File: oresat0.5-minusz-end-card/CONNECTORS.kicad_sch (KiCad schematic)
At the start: 25 parts, among them J2 Harwin M55-7101242R, J3 Harwin M55-7101242R, J4 Harwin M55-7101242R, J5 Harwin M55-7101242R

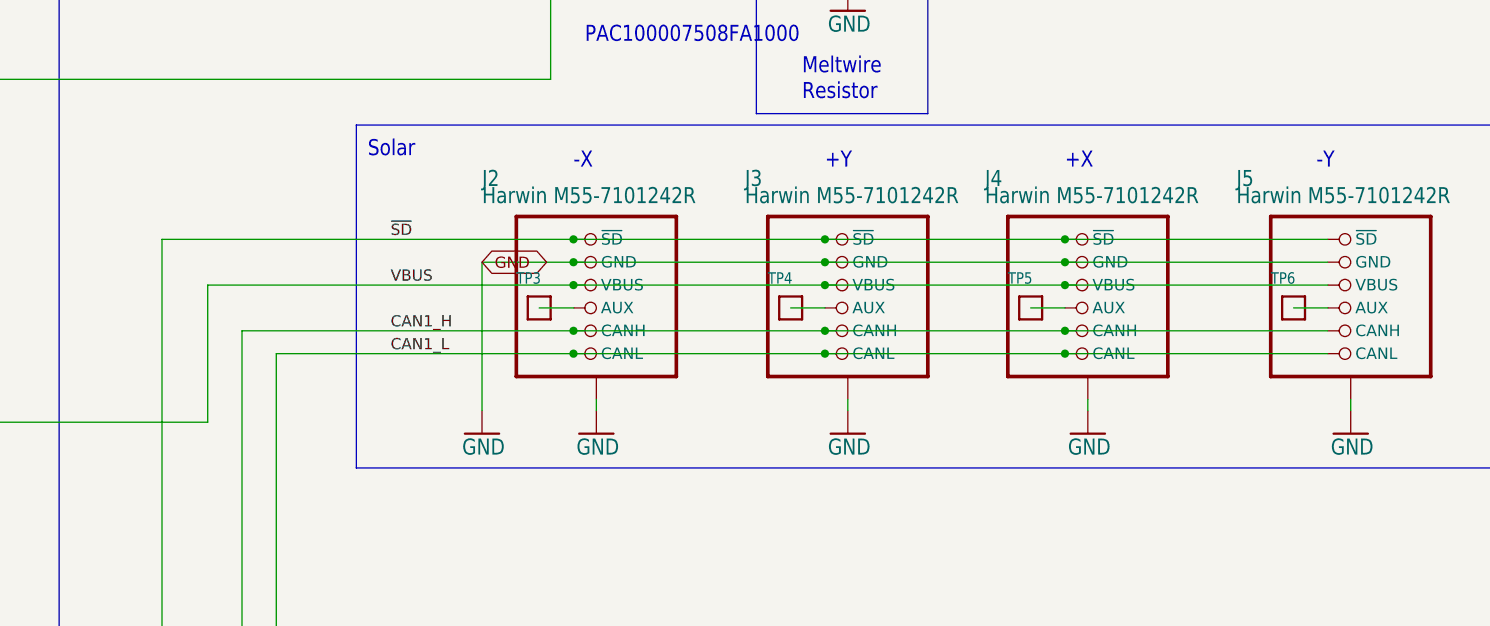
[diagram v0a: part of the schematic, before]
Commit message: Added new outline
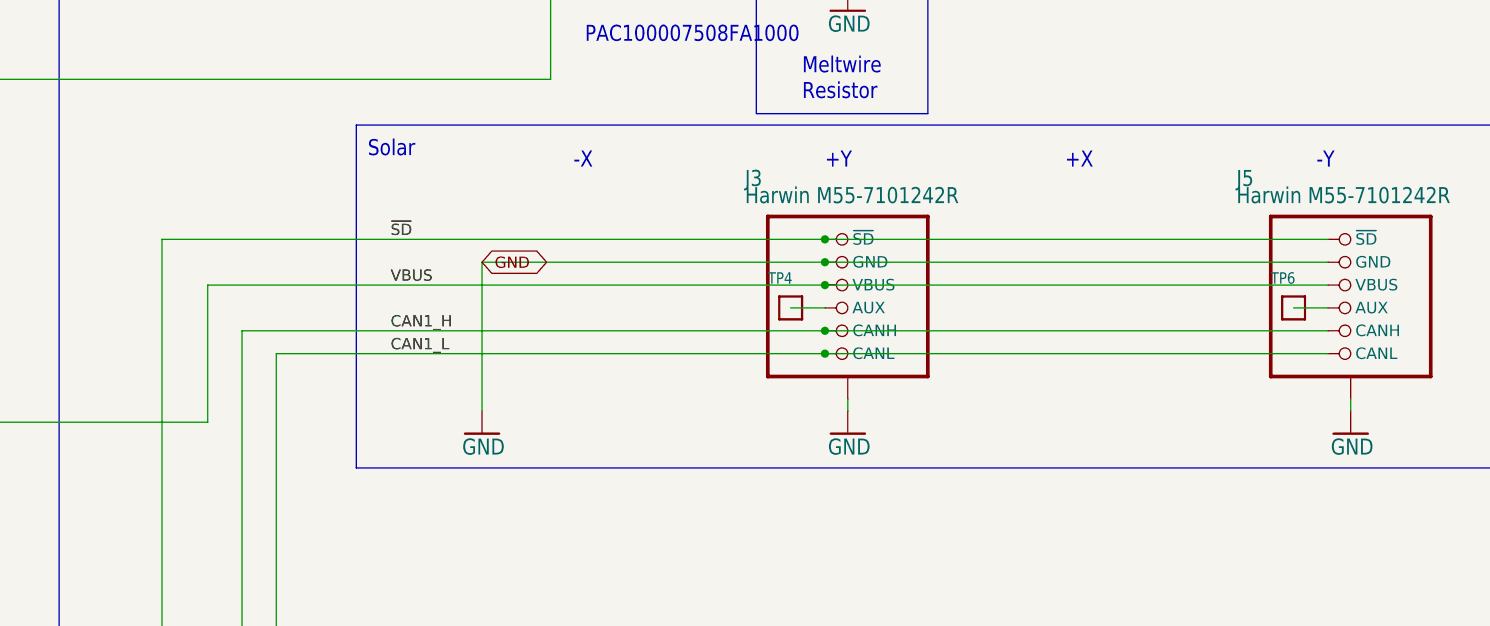
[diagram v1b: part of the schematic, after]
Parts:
- removed J2, J4: Harwin M55-7101242R, oresat-footprints:J-Harwin-M55-7101242R, symbol OreSat-j-solar-card-connector:SOLAR-CARD-CONNECTOR
- removed TP3, TP5: TEST-POINT-LARGE-SQUARE, plusz-end-card-with-turnstile:1X01, symbol plusz-end-card-with-turnstile-eagle-import:TEST-POINT-LARGE-SQUARE

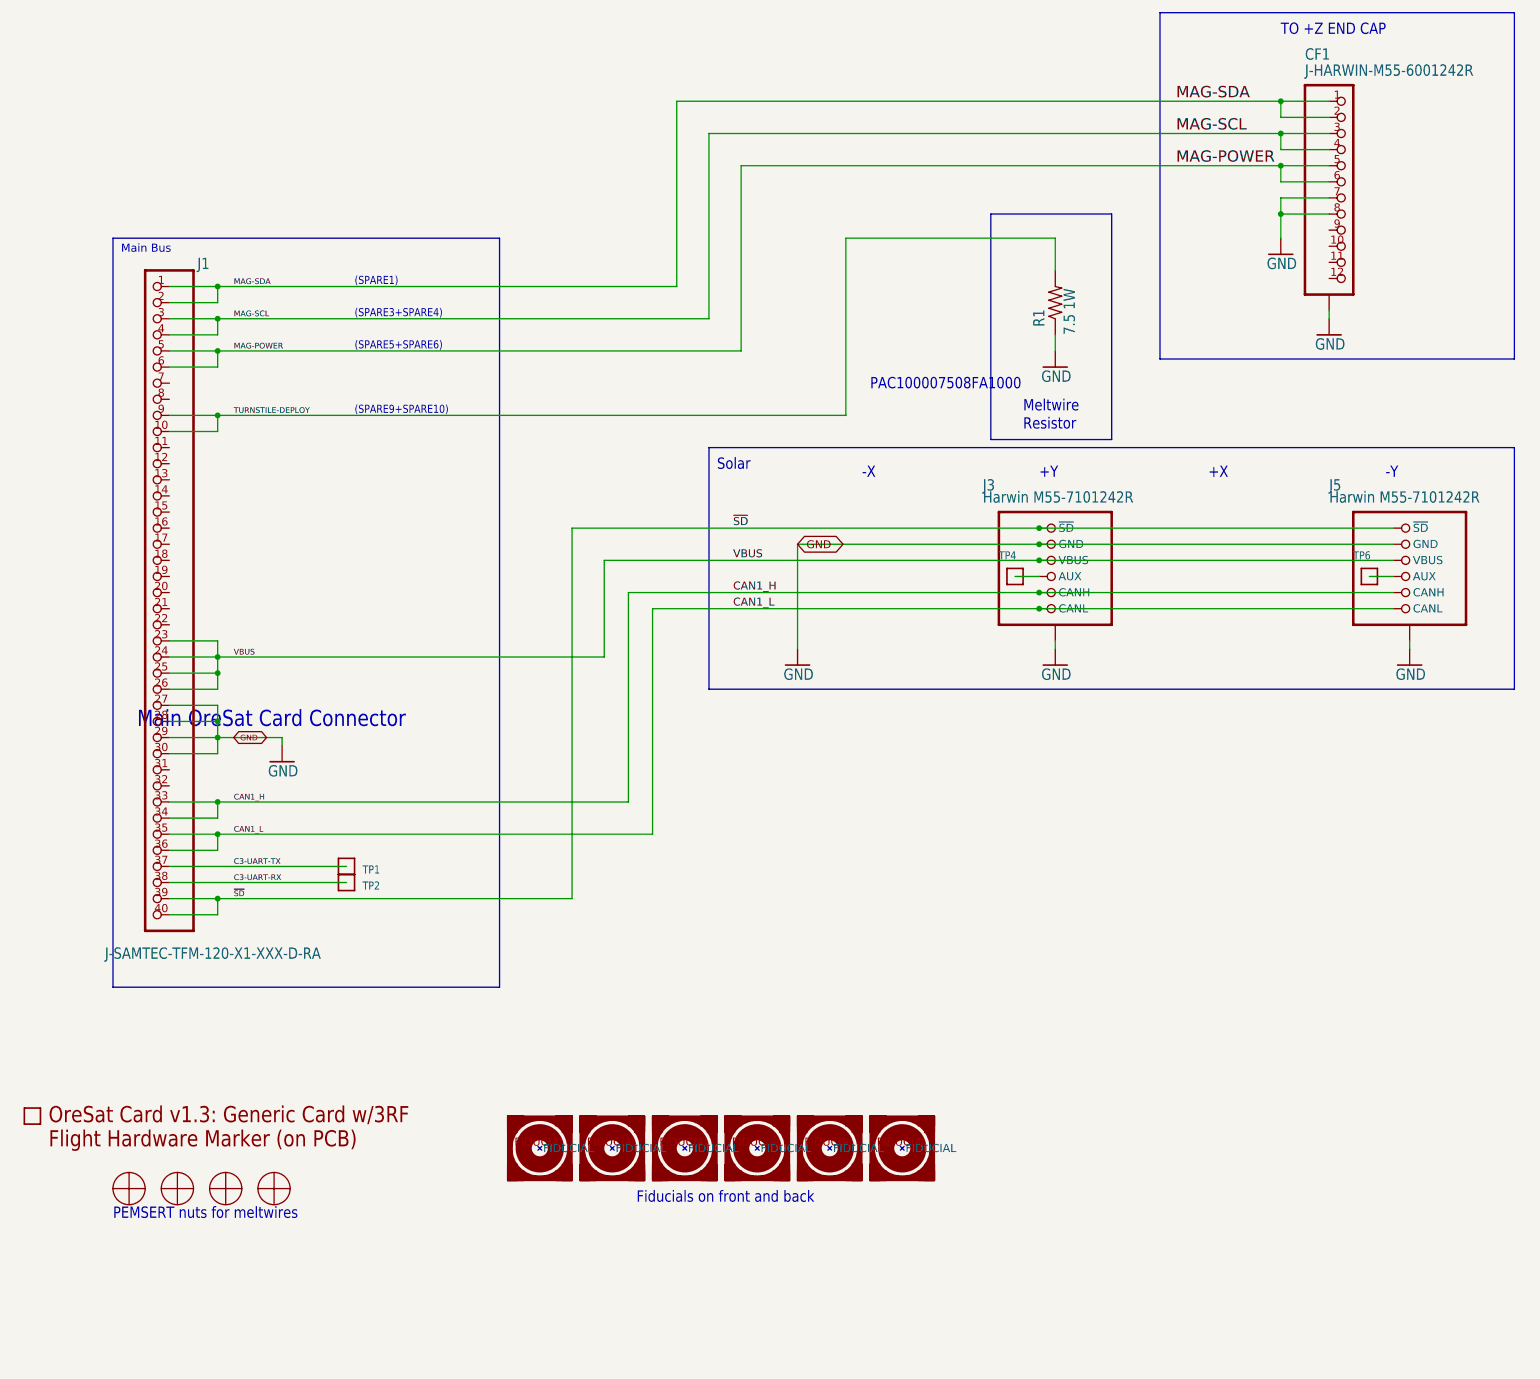
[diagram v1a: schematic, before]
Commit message: Updated -Z end card and replaced eagle imported libraries with kicad libraries
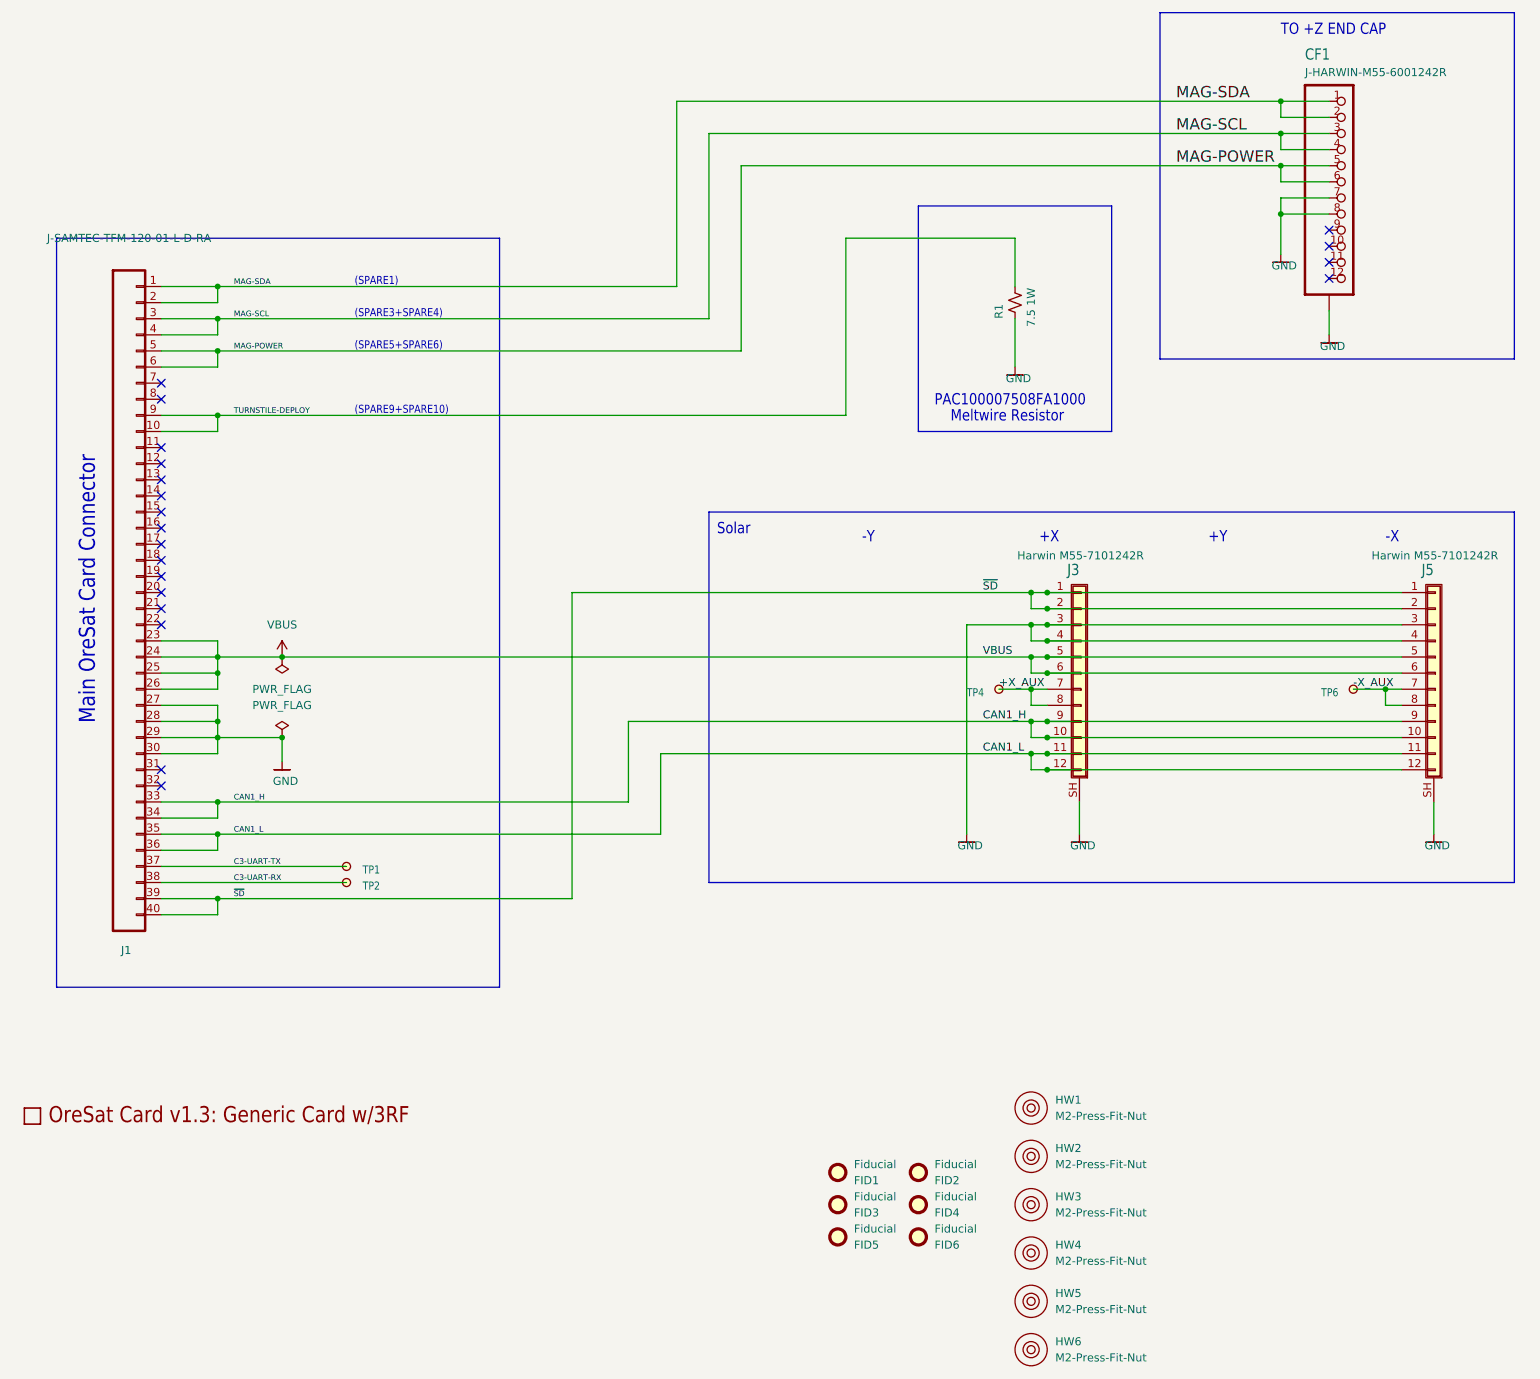
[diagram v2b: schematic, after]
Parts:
- removed HW1, HW2, HW3, HW4: MCMASTER-94100A150, oresat-footprints:H-MCMASTER-94100A150, symbol plusz-end-card-with-turnstile-eagle-import:MCMASTER-94100A150
- removed R1: 7.5 1W, oresat-footprints:R-PAC100-FOR-MELTWIRE, symbol plusz-end-card-with-turnstile-eagle-import:PAC100-FOR-MELTWIRE
- removed U$1: FLIGHMARKERNEW, plusz-end-card-with-turnstile:FLIGHTMARKER_NEW_BOARDS, symbol plusz-end-card-with-turnstile-eagle-import:FLIGHMARKERNEW
- added HW1, HW2, HW3, HW4, HW5, HW6: M2-Press-Fit-Nut, oresat-misc:M2-Press-Fit-Nut, symbol oresat-misc:M2-Press-Fit-Nut
- added R1: 7.5 1W, oresat-passives:R-PAC100-FOR-MELTWIRE, symbol Device:R_Small_US
- CF1: footprint plusz-end-card-with-turnstile:HARWIN-M55-60X1242R -> oresat-connectors:J-Harwin-M55-60X1242R; symbol plusz-end-card-with-turnstile-eagle-import:J-HARWIN-M55-60X1242R -> oresat-connectors:J-HARWIN-M55-6001242R
- FID1: renamed from FIDUCIAL1; value FIDUCIAL-1.0X2.0 -> Fiducial; footprint plusz-end-card-with-turnstile:FIDUCIAL-1.0X2.0 -> Fiducial:Fiducial_1mm_Mask2mm; symbol plusz-end-card-with-turnstile-eagle-import:FIDUCIAL-1.0X2.0 -> Mechanical:Fiducial
- FID2: renamed from FIDUCIAL2; value FIDUCIAL-1.0X2.0 -> Fiducial; footprint plusz-end-card-with-turnstile:FIDUCIAL-1.0X2.0 -> Fiducial:Fiducial_1mm_Mask2mm; symbol plusz-end-card-with-turnstile-eagle-import:FIDUCIAL-1.0X2.0 -> Mechanical:Fiducial
- FID3: renamed from FIDUCIAL3; value FIDUCIAL-1.0X2.0 -> Fiducial; footprint plusz-end-card-with-turnstile:FIDUCIAL-1.0X2.0 -> Fiducial:Fiducial_1mm_Mask2mm; symbol plusz-end-card-with-turnstile-eagle-import:FIDUCIAL-1.0X2.0 -> Mechanical:Fiducial
- FID4: renamed from FIDUCIAL4; value FIDUCIAL-1.0X2.0 -> Fiducial; footprint plusz-end-card-with-turnstile:FIDUCIAL-1.0X2.0 -> Fiducial:Fiducial_1mm_Mask2mm; symbol plusz-end-card-with-turnstile-eagle-import:FIDUCIAL-1.0X2.0 -> Mechanical:Fiducial
- FID5: renamed from FIDUCIAL5; value FIDUCIAL-1.0X2.0 -> Fiducial; footprint plusz-end-card-with-turnstile:FIDUCIAL-1.0X2.0 -> Fiducial:Fiducial_1mm_Mask2mm; symbol plusz-end-card-with-turnstile-eagle-import:FIDUCIAL-1.0X2.0 -> Mechanical:Fiducial
- FID6: renamed from FIDUCIAL6; value FIDUCIAL-1.0X2.0 -> Fiducial; footprint plusz-end-card-with-turnstile:FIDUCIAL-1.0X2.0 -> Fiducial:Fiducial_1mm_Mask2mm; symbol plusz-end-card-with-turnstile-eagle-import:FIDUCIAL-1.0X2.0 -> Mechanical:Fiducial
- J1: value (none) -> J-SAMTEC-TFM-120-01-L-D-RA; symbol plusz-end-card-with-turnstile-eagle-import:J-SAMTEC-TFM-120-X1-XXX-D-RA -> oresat-connectors:J-SAMTEC-TFM-120-01-L-D-RA
- J3, J5: footprint oresat-footprints:J-Harwin-M55-7101242R -> oresat-connectors:J-Harwin-M55-7101242R; symbol OreSat-j-solar-card-connector:SOLAR-CARD-CONNECTOR -> oresat-connectors:Harwin M55-7101242R
- TP1, TP2, TP4, TP6: footprint plusz-end-card-with-turnstile:1X01 -> oresat-misc:TestPoint-MinTH; symbol plusz-end-card-with-turnstile-eagle-import:TEST-POINT-LARGE-SQUARE -> oresat-misc:TestPoint-MinTH
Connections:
- net GND: now also CF1.SH (SHIELD), J3.SH (Shield), J5.SH (Shield), R1.2; no longer CF1.P$1 (SHIELDS), CF1.P$2 (SHIELDS), CF1.P$3 (SHIELDS), CF1.P$4 (SHIELDS), J3.GND (SHIELD), J5.GND (SHIELD)
- net TURNSTILE-DEPLOY: now also R1.1
- net -X_AUX: now reaches J5.7 (Pin_7), J5.8 (Pin_8), TP6.1
- net +X_AUX: now reaches J3.7 (Pin_7), J3.8 (Pin_8), TP4.1
- no-connect marks 0 -> 20
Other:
- note removed: "Fiducials on front and back"
- note removed: "Main Bus"
- note removed: "PEMSERT nuts for meltwires"
